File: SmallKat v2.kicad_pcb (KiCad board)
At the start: 4 copper layers, 100 x 56 mm, 142 parts, among them IC1 TPS562201DDCR, IC2 TPS562201DDCR, IC8 TPS40192DRCT-TPS40192DRCT, J1 Conn_01x03_Male, J10 Conn_01x03_Male, J11 Conn_01x03_Male, J12 Conn_01x03_Male, J13 Conn_01x03_Male, J14 Conn_01x03_Male, J15 Conn_01x03_Male, J16 Conn_01x03_Male, J17 Conn_01x03_Male, J18 Micro_SD_Card, J19 USB_C_Receptacle, J2 Conn_01x03_Male, J3 Conn_01x03_Male, J4 Conn_01x03_Male, J5 Conn_01x03_Male, J6 Conn_01x03_Male, J7 Conn_01x03_Male, J8 Conn_01x03_Male, J9 Conn_01x10_Female, Q1 BUK9M120-100EX, Q2 BUK9M120-100EX, Q3 MBT3904DW1, Q5 DMG2301L, SW1 SW_SPST, SW2 SW_SPST, U1 BNO055, U2 PCA9685BS, U3 ESP32-WROOM-32, U4 CP2102N-A01-GQFN24, Y1 32.768kHz

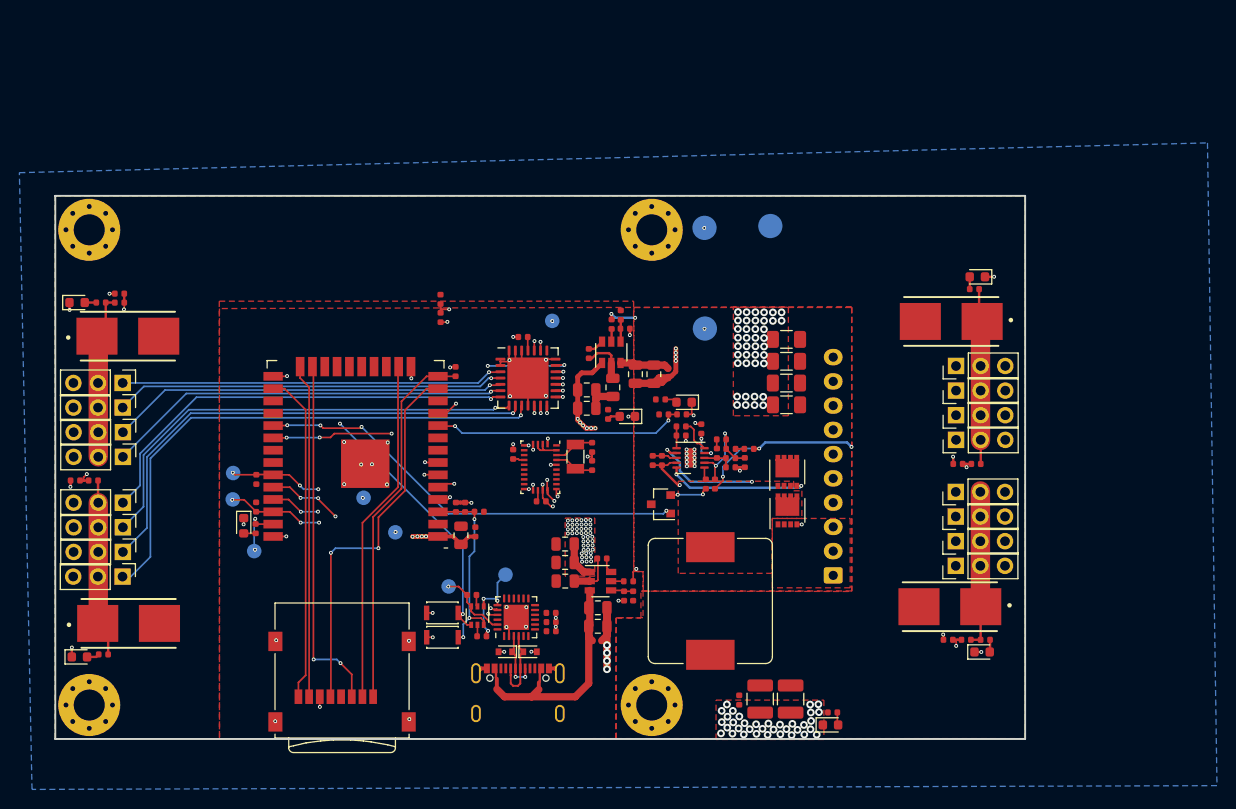
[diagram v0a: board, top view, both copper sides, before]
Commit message: batt connector and all in the right place. has not been ordered, waiting for prev rev to be tested first
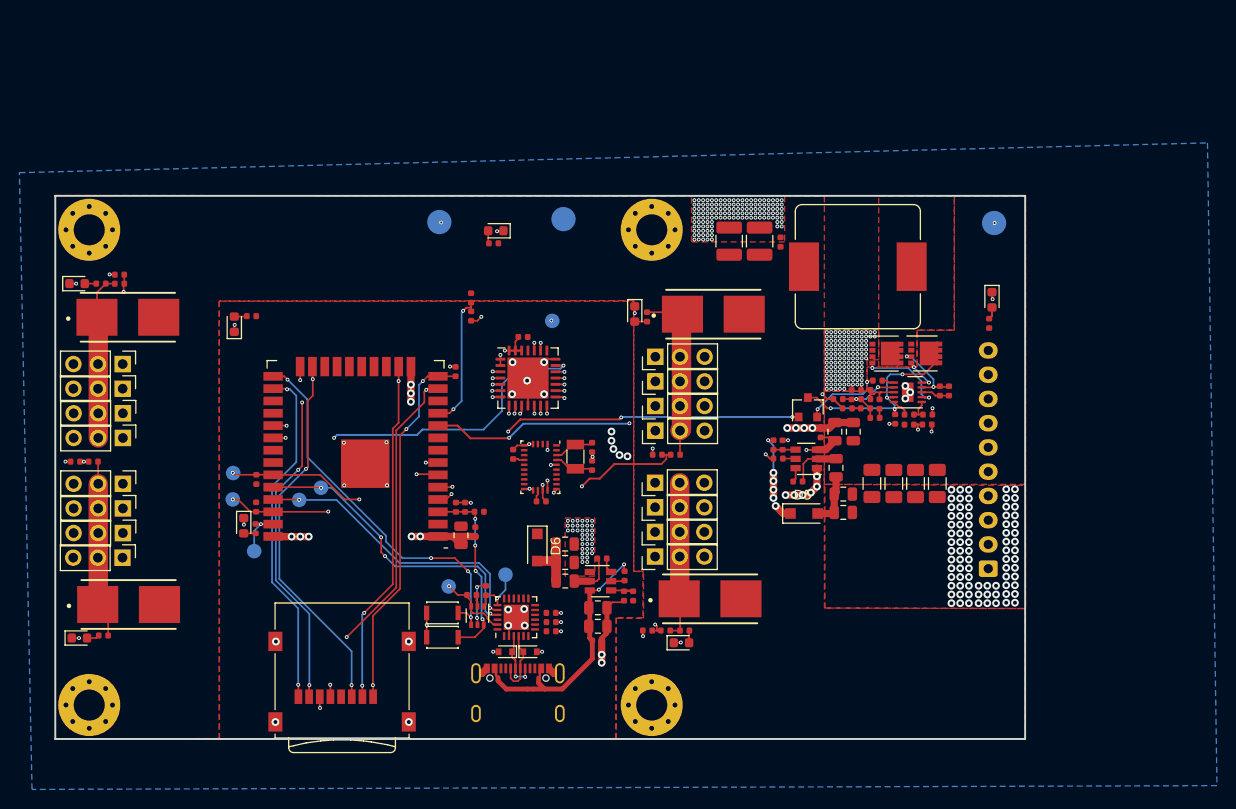
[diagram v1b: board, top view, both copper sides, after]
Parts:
- added D5: DIODE, Diode_SMD:D_SOD-123F, F.Cu at (145.3, 114.5)
- added D6: DIODE, Diode_SMD:D_SOD-123F, F.Cu at (117.8, 118.0)
- moved D4 61.5 mm to (113.6, 85.4), turned to 180 degrees
- moved R20 59.7 mm to (113.3, 86.7), turned to 180 degrees
- moved C19 47.6 mm to (137.6, 86.5), turned to 90 degrees
- moved C41 47.4 mm to (142.9, 86.6), turned to 90 degrees
- moved C21 47.2 mm to (140.8, 86.5), turned to 90 degrees
- moved D3 41.6 mm to (86.6, 95.0), turned to 90 degrees
- moved R7 38.1 mm to (88.4, 94.2), turned to 180 degrees
- moved L2 37.7 mm to (150.9, 89.1), turned to 180 degrees
- moved D26 35.5 mm to (127.9, 94.0), turned to 270 degrees
- moved R6 34.8 mm to (164.4, 94.9), turned to 90 degrees
- moved R86 33.9 mm to (129.2, 94.3), turned to 270 degrees
- moved D2 33.5 mm to (164.7, 92.5), turned to 270 degrees
- moved TP6 31.7 mm to (164.9, 84.6)
- moved R19 31.4 mm to (160.3, 101.9), turned to 270 degrees
- moved D25 31.0 mm to (132.7, 127.9)
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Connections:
- C23 pad 1: +3V3 -> Net-(C23-Pad1)
- C3 pad 1: +3V3 -> Net-(C3-Pad1)
- C30 pad 1: +3V3 -> Net-(C23-Pad1)
- C5 pad 1: +3V3 -> Net-(C3-Pad1)
- L1 pad 1: +3V3 -> Net-(C3-Pad1)
- L3 pad 1: +3V3 -> Net-(C23-Pad1)
- R30 pad 1: +BATT -> VBUS
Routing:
- net /MainBoard/SERVO8: track 55.0 -> 20.7 mm
- net MEASURED_FUSE4: track 59.5 -> 27.3 mm
- net /MainBoard/SERVO9: track 51.0 -> 19.1 mm
- net /MainBoard/SERVO13: track 42.9 -> 11.2 mm
- net /MainBoard/SERVO12: track 43.6 -> 12.0 mm
- net /MainBoard/SERVO14: track 42.0 -> 10.4 mm
- net /MainBoard/SERVO10: track 48.3 -> 16.9 mm
- net /MainBoard/SERVO15: track 41.5 -> 10.9 mm
- net /MainBoard/SERVO11: track 45.3 -> 16.5 mm
- net /MainBoard/BATT_VOLTAGE: track 26.1 -> 54.8 mm, vias 2 -> 3
- net MEASURED_FUSE3: track 61.7 -> 33.5 mm
- net +3V3: track 8.25 -> 31.6 mm, vias 1 -> 12
- net +BATT: track 13.4 -> 32.1 mm, vias 6 -> 7
- net GND: track 97.8 -> 81.1 mm, vias 205 -> 457
- net +6V: track 17.7 -> 2.91 mm, vias 4 -> 2
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
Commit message: rev, pendingorder
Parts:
- removed Q5: DMG2301L, Package_TO_SOT_SMD:SOT-23
- added D9: LED, LED_SMD:LED_0603_1608Metric, F.Cu at (106.8, 88.2)
- added F5: Fuse, 01550900M:0154.250DR, F.Cu at (105.1, 84.7)
- added J20: Conn_01x04_Female, Connector_JST:JST_SH_SM04B-SRSS-TB_1x04-1MP_P1.00mm_Horizontal, F.Cu at (85.0, 133.8)
- added J21: Conn_01x03_Male, Connector_PinHeader_2.54mm:PinHeader_1x03_P2.54mm_Vertical, F.Cu at (97.5, 88.8)
- added J22: Conn_01x03_Male, Connector_PinHeader_2.54mm:PinHeader_1x03_P2.54mm_Vertical, F.Cu at (92.3, 88.8)
- added J23: Conn_01x03_Male, Connector_PinHeader_2.54mm:PinHeader_1x03_P2.54mm_Vertical, F.Cu at (94.9, 88.7)
- added J24: Conn_01x03_Male, Connector_PinHeader_2.54mm:PinHeader_1x03_P2.54mm_Vertical, F.Cu at (89.8, 88.8)
- added R24: 8.2K, Resistor_SMD:R_0402_1005Metric, F.Cu at (102.5, 88.8)
- added R39: 20K, Resistor_SMD:R_0402_1005Metric, F.Cu at (104.4, 87.9)
- J18: footprint Connector_Card:microSD_HC_Wuerth_693072010801 -> Connector_Card:microSD_HC_Molex_104031-0811
- R17: value 100k -> 10K
- moved R17 52.1 mm to (102.5, 87.9)
- moved TP6 22.9 mm to (161.1, 107.2)
- moved TP4 8.00 mm to (115.8, 84.2)
- moved D4 5.44 mm to (118.6, 83.2)
- moved R20 5.44 mm to (118.3, 84.5)
- moved TP3 1.10 mm to (87.5, 113.0)
- moved TP7 0.96 mm to (121.5, 84.3)
- moved TP2 0.68 mm to (87.2, 110.5)
- moved J18 0.60 mm to (97.8, 131.3)
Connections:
- IC8 pad 1: Net-(IC8-Pad1) -> (no net)
- R17 pad 1: Net-(Q5-Pad2) -> /MainBoard/AD_6V
- R17 pad 2: Net-(IC8-Pad1) -> MEASURED_FUSE5
- U3 pad 27: (no net) -> /MainBoard/AD_SERVO_2
- U3 pad 28: (no net) -> /MainBoard/AD_SERVO_3
- U3 pad 29: /MainBoard/6VEN -> /MainBoard/AD_SERVO_1
- U3 pad 31: (no net) -> /MainBoard/AD_SERVO_4
- U3 pad 9: (no net) -> MEASURED_FUSE5
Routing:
- net /MainBoard/6VEN: track 55.4 -> 0.00 mm, vias 4 -> 0
- net /MainBoard/SDA: track 55.0 -> 81.8 mm, vias 4 -> 5
- net /MainBoard/SCL: track 52.2 -> 77.2 mm, vias 4 -> 5
- net /MainBoard/AD_SERVO_4: track 0.00 -> 22.8 mm, vias 0 -> 1
- net MEASURED_FUSE5: track 0.00 -> 21.8 mm, vias 0 -> 2
- net /MainBoard/AD_SERVO_1: track 0.00 -> 20.3 mm, vias 0 -> 1
- net /MainBoard/AD_6V: track 0.00 -> 20.1 mm
- net /MainBoard/AD_SERVO_3: track 0.00 -> 19.4 mm, vias 0 -> 1
- net /MainBoard/AD_SERVO_2: track 0.00 -> 19.0 mm, vias 0 -> 1
- net +BATT: track 32.1 -> 22.0 mm, vias 7 -> 6
- net Net-(Q5-Pad2): track 8.21 -> 0.00 mm, vias 2 -> 0
- net /MainBoard/IO15: track 38.6 -> 42.0 mm
- net /MainBoard/IO12: track 38.3 -> 41.6 mm, vias 3 -> 4
- net /MainBoard/IO4: track 35.9 -> 39.2 mm
- net /MainBoard/IO14: track 37.0 -> 40.3 mm
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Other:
- board text added: "+"
- board text added: "-"
- board text added: "3.3v"
- board text added: "3v"
- board text added: "6v"
- board text added: "Ankle"
- board text added: "Boot"
- board text added: "DTR"
- board text added: "EN"
- board text added: "Elbow"
- board text added: "Fuse"
- board text added: "GND"
- board text added: "IO 23"
- board text added: "Motherboard"
- board text added: "Pan"
- board text added: "RTS"
- board text added: "RX"
- board text added: "Rev ??"
- board text added: "SCL"
- board text added: "SDA"
- board text added: "Shoulder"
- board text added: "SmallKat"
- board text added: "TX"
- board text added: "Tilt"

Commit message: g
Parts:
- removed the C3 at (149.4, 114.4)
- removed the C5 at (149.4, 112.5)
- added C10: 22uF, Capacitor_SMD:C_0805_2012Metric, F.Cu at (149.4, 112.6)
- added C6: 22uF, Capacitor_SMD:C_0805_2012Metric, F.Cu at (149.4, 114.5)
- added J25: Conn_01x02_Female, RC-Battery-Connectors:XT-60_male, F.Cu at (163.8, 111.6)
- added J26: Conn_01x02_Female, RC-Battery-Connectors:XT-60_female, F.Cu at (117.5, 70.1)
- J1: renamed from J9; value Conn_01x10_Female -> DJI Battery Connector; moved to F.Cu
- J2: renamed from J20; value Conn_01x04_Female -> Qwiic connector
- Q2: renamed from Q1; value BUK9M120-100EX -> BUK9M17-30EX / BUK7M10-40E
- Q3: renamed from Q2; value BUK9M120-100EX -> BUK9M17-30EX / BUK7M10-40E
- R40: renamed from R16; value 3.9k -> 12k
- SW1, SW2: footprint Button_Switch_SMD:SW_SPST_CK_KXT3 -> Button_Switch_SMD:SW_SPST_EVQPE1
- TP1: value TestPoint -> Check for life
- TP10: renamed from TP7; value TestPoint -> GND
- TP11: renamed from TP4; value TestPoint -> 6V
- TP2: value TestPoint -> SDA
- TP3: value TestPoint -> SCL
- TP4: renamed from TP5; value TestPoint -> 3.3v
- TP9: renamed from TP6; value TestPoint -> Batt+
- moved J1 56.2 mm to (117.5, 78.0), turned to 180 degrees
- moved TP9 13.3 mm to (165.2, 94.5)
- moved R6 7.06 mm to (166.2, 101.8)
- moved D2 7.06 mm to (166.5, 99.3)
- moved SW1 6.05 mm to (102.6, 122.2)
- moved SW2 5.29 mm to (107.7, 132.6), turned to 90 degrees
- moved C30 0.18 mm to (156.7, 111.6)
- moved C32 0.18 mm to (154.5, 111.6)
- moved C34 0.18 mm to (152.2, 111.6)
- moved C31 0.18 mm to (159.0, 111.6)
- renumbered C17 to C1, C30 to C11, C6 to C12, C33 to C13, C7 to C14, C8 to C15, C9 to C16, C24 to C17, C26 to C18, C27 to C19, C1 to C2, C28 to C20, C29 to C21, C31 to C22, C32 to C23, C10 to C24, C11 to C25, C12 to C26, C13 to C27, C14 to C28, C15 to C29, C20 to C3, C16 to C30, C39 to C31, C18 to C32, C19 to C33, C40 to C34, C21 to C35, C41 to C36, C2 to C4, C22 to C5, C23 to C7, C4 to C8, C25 to C9, D24 to D10, D25 to D11, D26 to D12, D4 to D13, D9 to D3, D5 to D4, D6 to D5, D3 to D6, D23 to D9, F5 to F1, F1 to F2, F2 to F3, F3 to F4, F4 to F5, IC8 to IC3, J2 to J10, J3 to J11, J4 to J12, J5 to J13, J6 to J14, J7 to J15, J8 to J16, J10 to J17, J11 to J18, J12 to J19, J13 to J20, J14 to J21, J15 to J22, J16 to J23, J17 to J24, J21 to J3, J22 to J4, J23 to J5, J24 to J6, J18 to J7, J19 to J8, J1 to J9, L3 to L2, L2 to L3, Q3 to Q1, R8 to R10, R28 to R11, R9 to R12, R29 to R13, R10 to R14, R30 to R15, R7 to R16, R11 to R17, R21 to R18, R4 to R19, R5 to R20, R25 to R21, R26 to R22, R27 to R23, R31 to R24, R32 to R25, R63 to R26, R33 to R27, R34 to R28, R73 to R29, R35 to R30, R36 to R31, R78 to R32, R37 to R33, R38 to R34, R86 to R35, R12 to R36, R13 to R37, R14 to R38, R15 to R39, R22 to R4, R18 to R41, R19 to R42, R20 to R43, R23 to R5, R17 to R7, R24 to R8, R39 to R9, TP9 to TP5, TP10 to TP6, TP11 to TP7, TP12 to TP8, U2 to U1, U1 to U2
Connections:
- J1 pad 10: +BATT -> Net-(J1-Pad10)
- J1 pad 7: +BATT -> Net-(J1-Pad10)
- J1 pad 8: +BATT -> Net-(J1-Pad10)
- J1 pad 9: +BATT -> Net-(J1-Pad10)
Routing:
- net GND: track 83.3 -> 91.9 mm, vias 465 -> 491
- net /MainBoard/ESP32Module/IO0: track 39.0 -> 44.0 mm
- net /MainBoard/ESP32Module/EN: track 19.2 -> 23.1 mm
- net Net-(C10-Pad1): track 5.50 -> 6.52 mm
- added copper zone on In1.Cu, net GND
- added copper zone on B.Cu, net Net-(J1-Pad10)
- added copper zone on F.Cu, net Net-(J1-Pad10)
- added copper zone on In1.Cu, net Net-(J1-Pad10)
- added copper zone on In2.Cu, net Net-(J1-Pad10)
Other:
- board size 100 x 56 mm -> 100 x 72.3 mm
- board text added: "Batt"
- board text removed: "+"
- board text removed: "-"

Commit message: rev ordered
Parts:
- removed C10, C11, C7: 22uF, Capacitor_SMD:C_0805_2012Metric
- removed C13, C8, C9: 0.1uF, Capacitor_SMD:C_0402_1005Metric
- removed J1: DJI Battery Connector, Connector_JST:JST_EH_B10B-EH-A_1x10_P2.50mm_Vertical
- removed J26: Conn_01x02_Female, RC-Battery-Connectors:XT-60_female
- removed R14, R15: 10K, Resistor_SMD:R_0402_1005Metric
- added F6: Fuse, Fuse:Fuse_1210_3225Metric, F.Cu at (142.4, 107.1)
- added F7: Fuse, Fuse:Fuse_1210_3225Metric, F.Cu at (123.8, 115.3)
- added R44: 10K, Resistor_SMD:R_0402_1005Metric, F.Cu at (105.7, 97.5)
- added R45: 10K, Resistor_SMD:R_0402_1005Metric, F.Cu at (119.7, 96.5)
- added R46: 10K, Resistor_SMD:R_0402_1005Metric, F.Cu at (117.8, 95.4)
- added TP12: SDA, TestPoint:TestPoint_Pad_D1.5mm, B.Cu at (115.9, 94.6)
- added TP13: SCL, TestPoint:TestPoint_Pad_D1.5mm, B.Cu at (117.3, 91.7)
- C2, C5: value 10uF -> 2.2uF
- C3: value 10uF -> 0.1uF; footprint Capacitor_SMD:C_0805_2012Metric -> Capacitor_SMD:C_0402_1005Metric
- C6: value 22uF -> 10uF
- IC1, IC2: value TPS562201DDCR -> LMR50410YQDBVRQ1
- L1, L2: value 4.7uH -> 10uH
- R11: value 10K -> 23K
- R12: value 33.2K -> 23K
- R13: value 33.2K -> 10K
- moved C6 28.0 mm to (122.5, 122.4), turned to 180 degrees
- moved R10 9.95 mm to (147.4, 116.5), turned to 180 degrees
- moved R12 9.59 mm to (145.5, 116.5), turned to 0 degrees
- moved C4 9.07 mm to (146.0, 114.8), turned to 0 degrees
- moved R11 8.03 mm to (121.1, 128.7), turned to 0 degrees
- moved R13 7.48 mm to (121.5, 127.3), turned to 270 degrees
- moved D5 7.42 mm to (125.2, 119.1)
- moved C2 5.63 mm to (150.0, 111.7)
- moved IC2 5.22 mm to (124.0, 126.7)
- moved L2 4.73 mm to (125.2, 123.1), turned to 90 degrees
- moved L1 4.67 mm to (144.4, 111.8), turned to 270 degrees
- moved D4 4.16 mm to (142.4, 111.6), turned to 270 degrees
- moved C5 3.94 mm to (126.2, 129.5), turned to 0 degrees
- moved IC1 3.33 mm to (147.1, 111.9), turned to 90 degrees
- moved C12 1.88 mm to (144.9, 109.4)
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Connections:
- C2 pad 1: GND -> +BATT
- C2 pad 2: +BATT -> GND
- C3 pad 1: GND -> Net-(C3-Pad1)
- C3 pad 2: VBUS -> Net-(C3-Pad2)
- C4 pad 1: GND -> Net-(C4-Pad1)
- C4 pad 2: +BATT -> GND
- C5 pad 1: GND -> VBUS
- C5 pad 2: VBUS -> GND
- C6 pad 1: Net-(C10-Pad1) -> Net-(C6-Pad1)
- D4 pad 1: Net-(C10-Pad1) -> Net-(C4-Pad1)
- D4 pad 2: +3V3 -> Net-(D4-Pad2)
- D5 pad 1: Net-(C11-Pad1) -> Net-(C6-Pad1)
- D5 pad 2: +3V3 -> Net-(D5-Pad2)
- IC1 pad 1: GND -> Net-(C12-Pad2)
- IC1 pad 2: Net-(C12-Pad2) -> GND
- IC1 pad 3: +BATT -> Net-(IC1-Pad3)
- IC1 pad 4: Net-(IC1-Pad4) -> +BATT
- IC1 pad 5: Net-(IC1-Pad5) -> +BATT
- IC2 pad 1: GND -> Net-(C3-Pad2)
- IC2 pad 2: Net-(C13-Pad2) -> GND
- IC2 pad 3: VBUS -> Net-(IC2-Pad3)
- IC2 pad 4: Net-(IC2-Pad4) -> VBUS
- IC2 pad 5: Net-(IC2-Pad5) -> VBUS
- IC2 pad 6: Net-(C13-Pad1) -> Net-(C3-Pad1)
- L1 pad 1: Net-(C10-Pad1) -> Net-(C12-Pad1)
- L1 pad 2: Net-(C12-Pad2) -> Net-(C4-Pad1)
- L2 pad 1: Net-(C11-Pad1) -> Net-(C3-Pad1)
- L2 pad 2: Net-(C13-Pad2) -> Net-(C6-Pad1)
- R10 pad 2: Net-(IC1-Pad4) -> Net-(IC1-Pad3)
- R11 pad 1: GND -> +3V3
- R11 pad 2: Net-(IC2-Pad4) -> Net-(IC2-Pad3)
- R12 pad 2: Net-(IC1-Pad4) -> Net-(IC1-Pad3)
- R13 pad 1: +3V3 -> GND
- R13 pad 2: Net-(IC2-Pad4) -> Net-(IC2-Pad3)
- U1 pad 23: /MainBoard/SCL -> /MainBoard/SCL_1
- U1 pad 24: /MainBoard/SDA -> /MainBoard/SDA_1
- U3 pad 12: (no net) -> /MainBoard/SCL_1
- U3 pad 8: (no net) -> /MainBoard/SDA_1
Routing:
- net /MainBoard/SDA_1: track 0.00 -> 23.9 mm, vias 0 -> 2
- net /MainBoard/SCL_1: track 0.00 -> 23.7 mm, vias 0 -> 2
- net /MainBoard/SDA: track 81.8 -> 63.1 mm, vias 5 -> 4
- net /MainBoard/SCL: track 77.2 -> 60.8 mm, vias 5 -> 4
- net GND: track 91.9 -> 76.1 mm, vias 491 -> 425
- net +3V3: track 31.6 -> 40.2 mm, vias 12 -> 11
- net +BATT: track 22.0 -> 14.2 mm, vias 6 -> 4
- net Net-(IC1-Pad3): track 0.00 -> 7.29 mm, vias 0 -> 2
- net VBUS: track 27.8 -> 20.6 mm, vias 2 -> 0
- net Net-(C10-Pad1): track 6.52 -> 0.00 mm
- net Net-(C11-Pad1): track 5.82 -> 0.00 mm
- net Net-(C13-Pad2): track 4.80 -> 0.00 mm
- net Net-(C4-Pad1): track 0.00 -> 4.29 mm
- net /MainBoard/IO12: track 41.6 -> 45.1 mm
- net Net-(C6-Pad1): track 0.00 -> 3.37 mm
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- removed copper zone on In1.Cu, net GND
- removed copper zone on B.Cu, net Net-(J1-Pad10)
- removed copper zone on F.Cu, net Net-(J1-Pad10)
- removed copper zone on In1.Cu, net Net-(J1-Pad10)
- removed copper zone on In2.Cu, net Net-(J1-Pad10)
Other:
- board size 100 x 72.3 mm -> 100 x 56 mm
- net class Default: via_dia 0.4 -> 0.45; via_drill 0.2 -> 0.3
- board text added: "SCL 1"
- board text added: "SDA 1"
